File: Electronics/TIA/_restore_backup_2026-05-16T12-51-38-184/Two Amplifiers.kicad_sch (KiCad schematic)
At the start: 3 parts, among them U1 ${SIM.PARAMS}

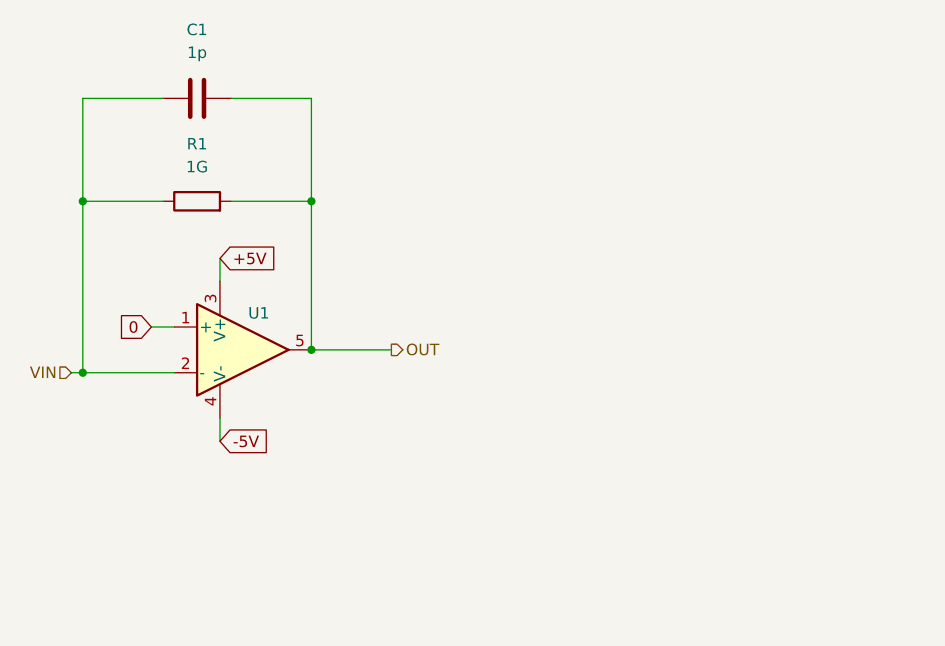
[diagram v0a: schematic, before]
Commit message: Create a robust TIA design following the requirements
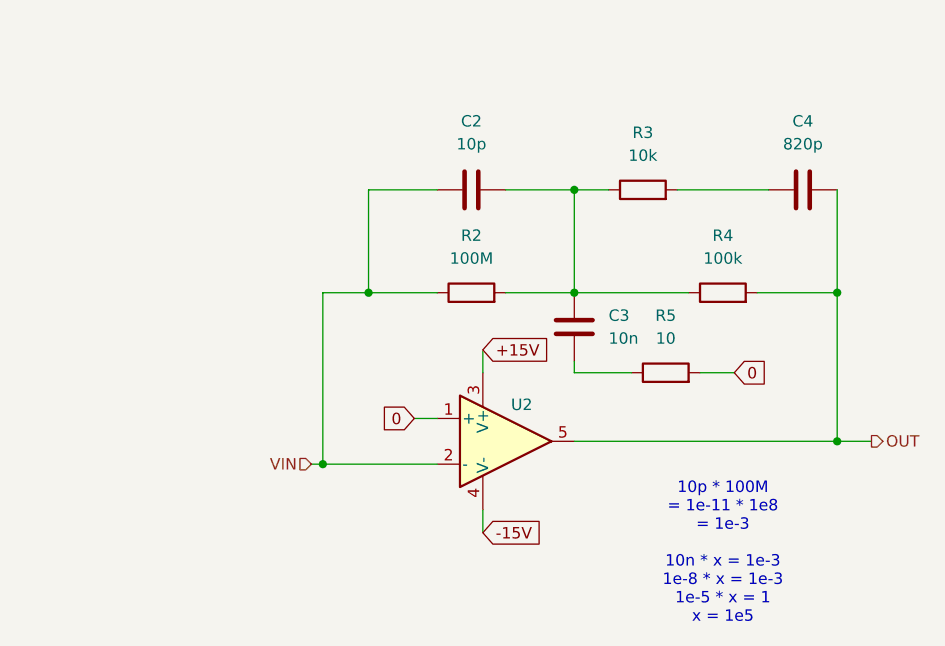
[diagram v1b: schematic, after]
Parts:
- removed C1: 1p, symbol Device:C
- removed R1: 1G, symbol Device:R
- removed U1: ${SIM.PARAMS}, symbol Simulation_SPICE:OPAMP
- added C2: 10p, symbol Device:C
- added C3: 10n, symbol Device:C
- added C4: 820p, symbol Device:C
- added R2: 100M, symbol Device:R
- added R3: 10k, symbol Device:R
- added R4: 100k, symbol Device:R
- added R5: 10, symbol Device:R
- added U2: ${SIM.PARAMS}, symbol Simulation_SPICE:OPAMP
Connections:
- net 0: now also R5.2, U2.1 (+)
- net OUT: now also C4.2, R4.2, U2.5
- net VIN: now also C2.1, R2.1, U2.2 (-)
- new net: C4.1, R3.2
- new net: C2.2, C3.2, R2.2, R3.1, R4.1
- new net: C3.1, R5.1
- new net +15V: U2.3 (V+)
- new net -15V: U2.4 (V-)
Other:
- note added: "10p * 100M = 1e-11 * 1e8 = 1e-3 10n * x = 1e-3 1e-8 * x = 1e-3 1e-5 * x = 1 x = 1e5"
